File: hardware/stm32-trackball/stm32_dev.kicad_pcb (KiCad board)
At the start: 2 copper layers, 70.8 x 30 mm, 54 parts, among them J1 USB_C_Receptacle_USB2.0, J2 SWD, J3 UART, J4 SPARE, J5 Breakout, J6 Breakout, SW1 SIDE, SW2 SIDE, SW3 SW_Push, T1 Trackball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

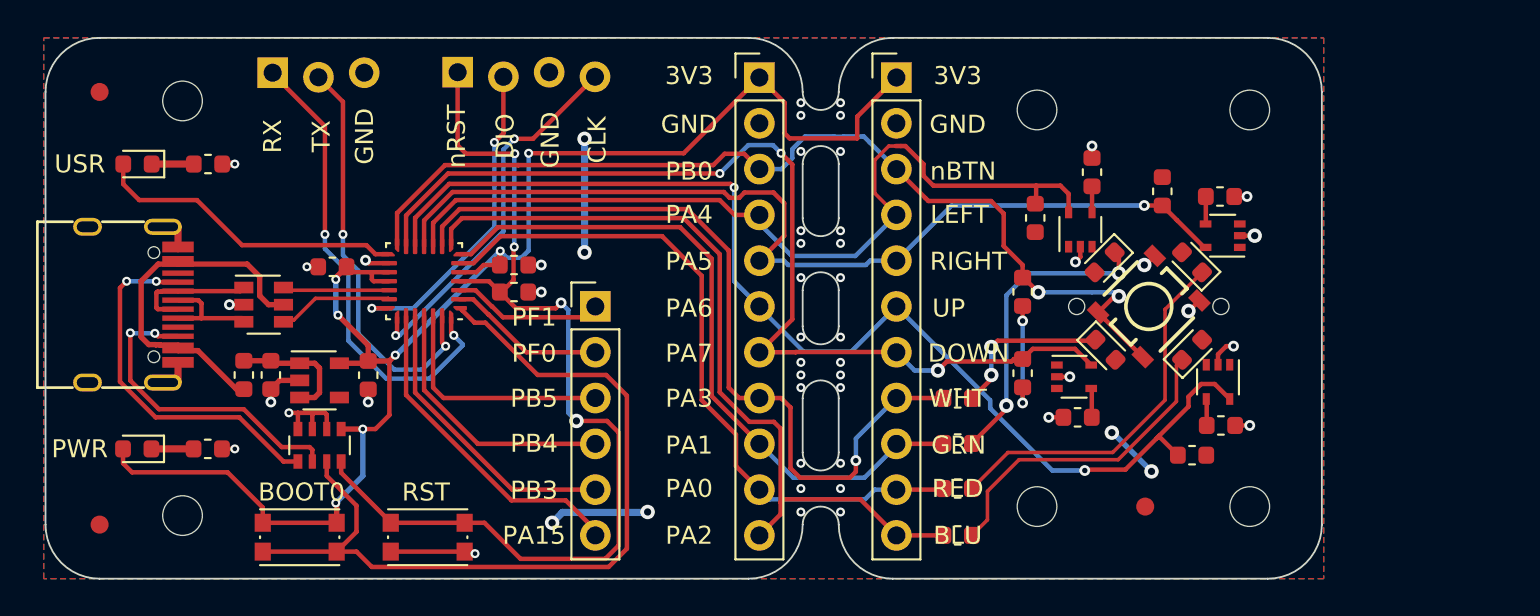
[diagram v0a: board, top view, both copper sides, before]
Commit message: added extra buttons
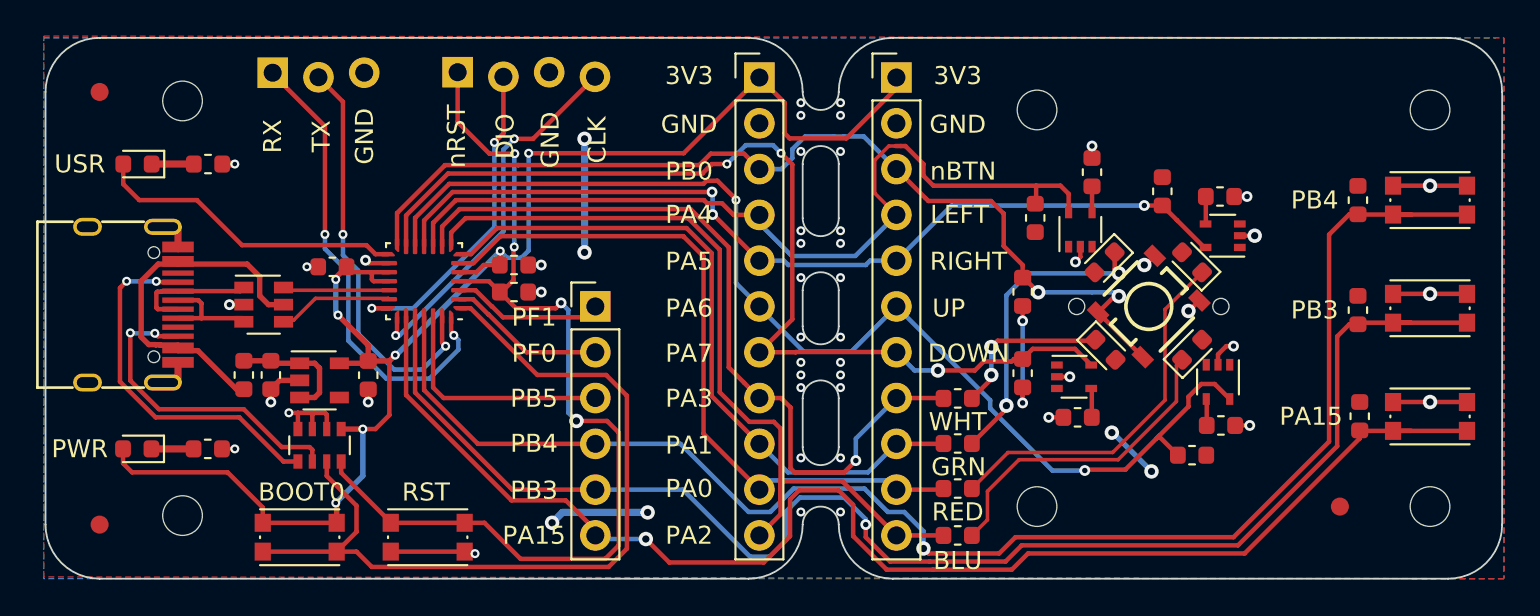
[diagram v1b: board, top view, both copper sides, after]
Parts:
- added R12: 10K, Resistor_SMD:R_0603_1608Metric, F.Cu at (142.8, 95.0)
- added R13: 10K, Resistor_SMD:R_0603_1608Metric, F.Cu at (142.8, 101.1)
- added R14: 10K, Resistor_SMD:R_0603_1608Metric, F.Cu at (142.9, 107.0)
- added SW4: KMR2, josh-buttons-switches:SW_Push_KMR2, F.Cu at (146.8, 95.0)
- added SW5: KMR2, josh-buttons-switches:SW_Push_KMR2, F.Cu at (146.8, 101.0)
- added SW6: KMR2, josh-buttons-switches:SW_Push_KMR2, F.Cu at (146.8, 107.0)
- SW1, SW2: value SIDE -> KMR2
- moved H1 10.8 mm to (141.8, 112.0)
- moved H8 10.0 mm to (146.8, 90.0)
- moved H9 10.0 mm to (146.8, 112.0)
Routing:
- net /SPARE_4: track 14.8 -> 82.9 mm, vias 0 -> 1
- net /SPARE_5: track 16.5 -> 81.1 mm, vias 0 -> 1
- net /SPARE_6: track 18.3 -> 77.5 mm, vias 0 -> 1
- net GND: track 31.5 -> 43.8 mm, vias 31 -> 32
- net /TB_UP: track 53.5 -> 50.2 mm, vias 1 -> 3
- net /nLED_BLU: track 44.9 -> 46.4 mm
- net /nLED_WHT: track 44.6 -> 43.6 mm
- net /nRST: track 56.0 -> 55.2 mm
- net /nLED_RED: track 38.7 -> 39.3 mm
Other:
- board size 70.8 x 30 mm -> 80.8 x 30 mm

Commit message: off to fab
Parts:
- added H10: Title, josh-logos:board-title, B.Cu at (133.9, 89.4)
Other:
- rule pad_to_mask_clearance: 0.05 -> 0
- rule via_min_drill: 0.3 -> 0.25
- rule via_min_size: 0.4 -> 0.5
- board text added: "JLCJLCJLC"

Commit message: Fast forward to KiCad 7 ;)
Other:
- net class Default removed
